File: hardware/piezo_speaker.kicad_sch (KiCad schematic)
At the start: 4 parts, among them Q2 2N3904

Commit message: Removed comments on UART, added some footprints and started fixing rule checks
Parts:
- LS2: Manuf. Name (none) -> TDK; Manuf. Part # (none) -> PS1240P02CT3; Manufacturer_Name TDK -> (none); Manufacturer_Part_Number PS1240P02CT3 -> (none); Part Num C76873 -> (none); Price/unit $0.2409 -> (none); Supplier Name (none) -> JLCPCB; Supplier Unit Price (none) -> $0.2409
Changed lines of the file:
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@@
-			)
-		)
-		(property "Manufacturer_Name" "TDK"
-			(at 161.29 592.71 0)
-			(effects
-				(font
-					(size 1.27 1.27)
-				)
-				(justify left top)
-				(hide yes)
-			)
-		)
-		(property "Manufacturer_Part_Number" "PS1240P02CT3"
-			(at 161.29 692.71 0)
-			(effects
-				(font
-					(size 1.27 1.27)
-				)
-				(justify left top)
-				(hide yes)
-			)
-		)
-		(property "Mouser Part Number" ""
-			(at 161.29 792.71 0)
-			(effects
-				(font
-					(size 1.27 1.27)
-				)
-				(justify left top)
-				(hide yes)
-			)
-		)
-		(property "Mouser Price/Stock" ""
-			(at 161.29 892.71 0)
-			(effects
-				(font
-					(size 1.27 1.27)
-				)
-				(justify left top)
-				(hide yes)
 			)
 		)
@@
 			)
 		)
-		(property "Price/unit" " $0.2409"
-			(at 149.86 90.17 0)
-			(effects
-				(font
-					(size 1.27 1.27)
-				)
-				(hide yes)
-			)
-		)
-		(property "Part Num" "C76873"
-			(at 149.86 90.17 0)
-			(effects
-				(font
-					(size 1.27 1.27)
-				)
-				(hide yes)
-			)
-		)
 		(property "Package" "Plugin,D=12.2mm"
+			(at 149.86 90.17 0)
+			(effects
+				(font
+					(size 1.27 1.27)
+				)
+				(hide yes)
+			)
+		)
+		(property "Manuf. Name" "TDK"
+			(at 149.86 90.17 0)
+			(effects
+				(font
+					(size 1.27 1.27)
+				)
+				(hide yes)
+			)
+		)
+		(property "Manuf. Part #" "PS1240P02CT3"
+			(at 149.86 90.17 0)
+			(effects
+				(font
+					(size 1.27 1.27)
+				)
+				(hide yes)
+			)
+		)
+		(property "Supplier Name" "JLCPCB"
+			(at 149.86 90.17 0)
+			(effects
+				(font
+					(size 1.27 1.27)
+				)
+				(hide yes)
+			)
+		)
+		(property "Supplier Unit Price" " $0.2409"
 			(at 149.86 90.17 0)
 			(effects
@@
 			)
 		)
+		(property "Supplier Name" ""
+			(at 143.51 91.44 0)
+			(effects
+				(font
+					(size 1.27 1.27)
+				)
+				(hide yes)
+			)
+		)
 		(pin "1"
 		)
@@
 		)
 		(property "Description" "Resistor, small symbol"
+			(at 135.89 102.87 0)
+			(effects
+				(font
+					(size 1.27 1.27)
+				)
+				(hide yes)
+			)
+		)
+		(property "Supplier Name" ""
 			(at 135.89 102.87 0)
 			(effects
@@
 			(at 147.32 102.87 0)
 			(effects
+				(font
+					(size 1.27 1.27)
+				)
+				(hide yes)
+			)
+		)
+		(property "Supplier Name" ""
+			(at 147.32 102.87 0)
+			(effects

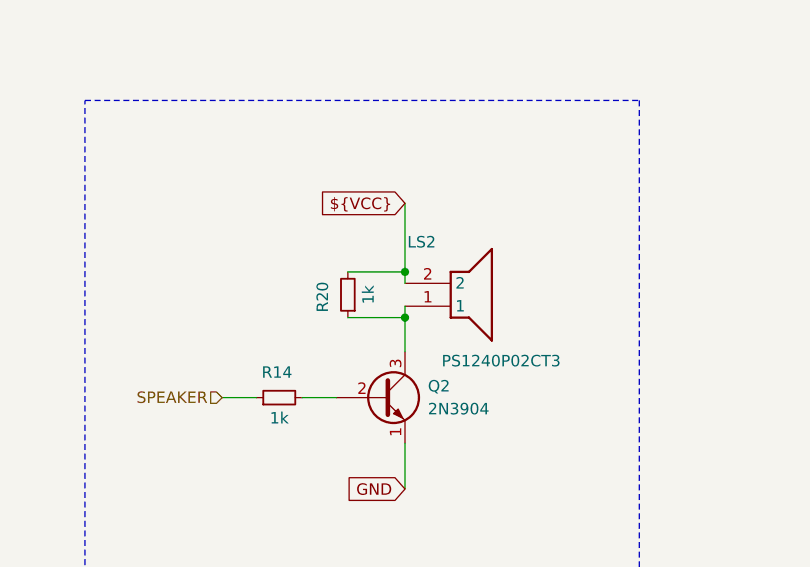
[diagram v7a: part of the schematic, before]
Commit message: Added many footprints and populated part of the property tables
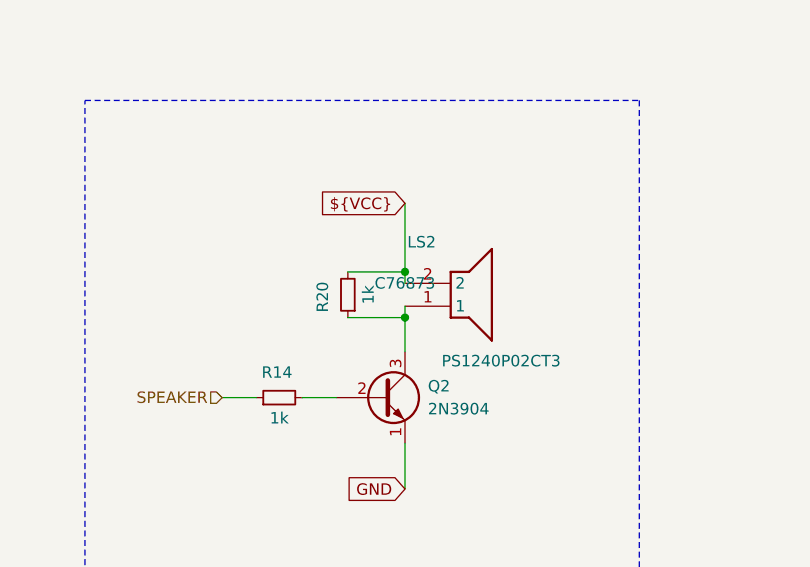
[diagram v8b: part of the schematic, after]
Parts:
- LS2: footprint (none) -> kitchen_timer:PS1240P02BT; Supplier Part # (none) -> C76873; Supplier Unit Price $0.2409 -> $0.2462; now left out of the parts list
- R14, R20: footprint (none) -> Resistor_SMD:R_0805_2012Metric_Pad1.20x1.40mm_HandSolder; Manuf. Name (none) -> UNI-ROYAL(Uniroyal Elec); Manuf. Part # (none) -> 0805W8F1001T5E; Package (none) -> 0805; Supplier Link (none) -> https://jlcpcb.com/partdetail/18201-0805W8F1001T5E/C17513; Supplier Name (none) -> JLCPCB; Supplier Part # (none) -> C17513; Supplier Unit Price (none) -> $0.0017
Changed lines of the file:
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@@
 		(unit 1)
 		(exclude_from_sim no)
-		(in_bom yes)
+		(in_bom no)
 		(on_board yes)
 		(dnp no)
@@
 			)
 		)
-		(property "Footprint" ""
+		(property "Footprint" "kitchen_timer:PS1240P02BT"
 			(at 161.29 192.71 0)
 			(effects
@@
 			)
 		)
-		(property "Supplier Unit Price" " $0.2409"
-			(at 149.86 90.17 0)
-			(effects
-				(font
-					(size 1.27 1.27)
-				)
-				(hide yes)
+		(property "Supplier Unit Price" " $0.2462"
+			(at 149.86 90.17 0)
+			(effects
+				(font
+					(size 1.27 1.27)
+				)
+				(hide yes)
+			)
+		)
+		(property "Supplier Part #" " C76873"
+			(at 149.86 90.17 0)
+			(effects
+				(font
+					(size 1.27 1.27)
+				)
 			)
 		)
@@
 			)
 		)
-		(property "Footprint" ""
-			(at 143.51 91.44 0)
-			(effects
-				(font
-					(size 1.27 1.27)
-				)
-				(hide yes)
-			)
-		)
-		(property "Datasheet" "~"
-			(at 143.51 91.44 0)
-			(effects
-				(font
-					(size 1.27 1.27)
-				)
-				(hide yes)
-			)
-		)
-		(property "Description" "Resistor, small symbol"
-			(at 143.51 91.44 0)
-			(effects
-				(font
-					(size 1.27 1.27)
-				)
-				(hide yes)
-			)
-		)
-		(property "Supplier Name" ""
+		(property "Footprint" "Resistor_SMD:R_0805_2012Metric_Pad1.20x1.40mm_HandSolder"
+			(at 143.51 91.44 0)
+			(effects
+				(font
+					(size 1.27 1.27)
+				)
+				(hide yes)
+			)
+		)
+		(property "Datasheet" "https://jlcpcb.com/api/file/downloadByFileSystemAccessId/8579706499683172352"
+			(at 143.51 91.44 0)
+			(effects
+				(font
+					(size 1.27 1.27)
+				)
+				(hide yes)
+			)
+		)
+		(property "Description" "1k, 0805"
+			(at 143.51 91.44 0)
+			(effects
+				(font
+					(size 1.27 1.27)
+				)
+				(hide yes)
+			)
+		)
+		(property "Supplier Name" "JLCPCB"
+			(at 143.51 91.44 0)
+			(effects
+				(font
+					(size 1.27 1.27)
+				)
+				(hide yes)
+			)
+		)
+		(property "Manuf. Name" "UNI-ROYAL(Uniroyal Elec)"
+			(at 143.51 91.44 0)
+			(effects
+				(font
+					(size 1.27 1.27)
+				)
+				(hide yes)
+			)
+		)
+		(property "Manuf. Part #" "0805W8F1001T5E"
+			(at 143.51 91.44 0)
+			(effects
+				(font
+					(size 1.27 1.27)
+				)
+				(hide yes)
+			)
+		)
+		(property "Package" "0805"
+			(at 143.51 91.44 0)
+			(effects
+				(font
+					(size 1.27 1.27)
+				)
+				(hide yes)
+			)
+		)
+		(property "Supplier Link" "https://jlcpcb.com/partdetail/18201-0805W8F1001T5E/C17513"
+			(at 143.51 91.44 0)
+			(effects
+				(font
+					(size 1.27 1.27)
+				)
+				(hide yes)
+			)
+		)
+		(property "Supplier Part #" "C17513"
+			(at 143.51 91.44 0)
+			(effects
+				(font
+					(size 1.27 1.27)
+				)
+				(hide yes)
+			)
+		)
+		(property "Supplier Unit Price" "$0.0017"
 			(at 143.51 91.44 0)
 			(effects
@@
 			)
 		)
-		(property "Footprint" ""
-			(at 135.89 102.87 0)
-			(effects
-				(font
-					(size 1.27 1.27)
-				)
-				(hide yes)
-			)
-		)
-		(property "Datasheet" "~"
-			(at 135.89 102.87 0)
-			(effects
-				(font
-					(size 1.27 1.27)
-				)
-				(hide yes)
-			)
-		)
-		(property "Description" "Resistor, small symbol"
-			(at 135.89 102.87 0)
-			(effects
-				(font
-					(size 1.27 1.27)
-				)
-				(hide yes)
-			)
-		)
-		(property "Supplier Name" ""
-			(at 135.89 102.87 0)
-			(effects
+		(property "Footprint" "Resistor_SMD:R_0805_2012Metric_Pad1.20x1.40mm_HandSolder"
+			(at 135.89 102.87 0)
+			(effects
+				(font
+					(size 1.27 1.27)
+				)
+				(hide yes)
+			)
+		)
+		(property "Datasheet" "https://jlcpcb.com/api/file/downloadByFileSystemAccessId/8579706499683172352"
+			(at 135.89 102.87 0)
+			(effects
+				(font
+					(size 1.27 1.27)
+				)
+				(hide yes)
+			)
+		)
+		(property "Description" "1k, 0805"
+			(at 135.89 102.87 0)
+			(effects
+				(font
+					(size 1.27 1.27)
+				)
+				(hide yes)
+			)
+		)
+		(property "Supplier Name" "JLCPCB"
+			(at 135.89 102.87 0)
+			(effects
+				(font
+					(size 1.27 1.27)
+				)
+				(hide yes)
+			)
+		)
+		(property "Manuf. Name" "UNI-ROYAL(Uniroyal Elec)"
+			(at 135.89 102.87 0)
+			(effects
+				(font
+					(size 1.27 1.27)
+				)
+				(hide yes)
+			)
+		)
+		(property "Manuf. Part #" "0805W8F1001T5E"
+			(at 135.89 102.87 0)
+			(effects
+				(font
+					(size 1.27 1.27)
+				)
+				(hide yes)
+			)
+		)
+		(property "Package" "0805"
+			(at 135.89 102.87 0)
+			(effects
+				(font
+					(size 1.27 1.27)
+				)
+				(hide yes)
+			)
+		)
+		(property "Supplier Link" "https://jlcpcb.com/partdetail/18201-0805W8F1001T5E/C17513"
+			(at 135.89 102.87 0)
+			(effects
+				(font
+					(size 1.27 1.27)
+				)
+				(hide yes)
+			)
+		)
+		(property "Supplier Part #" "C17513"
+			(at 135.89 102.87 0)
+			(effects
+				(font
+					(size 1.27 1.27)
+				)
+				(hide yes)
+			)
+		)
+		(property "Supplier Unit Price" "$0.0017"
+			(at 135.89 102.87 0)
+			(effects
